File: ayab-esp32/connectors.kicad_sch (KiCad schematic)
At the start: 0 parts

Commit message: first draft schematic
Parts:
- added J602: 900_SOLENOIDS_A, symbol Connector_Generic:Conn_01x10
- added J603: 900_SOLENOIDS_B, symbol Connector_Generic:Conn_01x08
- added J604: USER_I2C, symbol Connector_Generic:Conn_01x04
- added J605: USER_SPI, symbol Connector_Generic:Conn_01x05
- added J606: 910_SOLENOIDS_A, symbol Connector_Generic:Conn_01x10
- added J607: 910_SOLENOIDS_B, symbol Connector_Generic:Conn_01x08
- added J608: 910_ENCODERS_EOL_R, symbol Connector_Generic:Conn_01x10
- added J609: USER_UART, symbol Connector_Generic:Conn_01x04
- added J610: 930_SOLENOIDS_A, symbol Connector_Generic:Conn_01x10
- added J611: 930_SOLENOIDS_B, symbol Connector_Generic:Conn_01x08
- added J612: 930_910_EOL_L, symbol Connector_Generic:Conn_01x03
- added J613: 930_EOL_R, symbol Connector_Generic:Conn_01x03
- added J614: 930_ENCODERS, symbol Connector_Generic:Conn_01x05
- added J615: 965_EOL_L, symbol Connector_Generic:Conn_01x03
- added J616: 965_EOL_R, symbol Connector_Generic:Conn_01x03
- added J617: 965_ENCODERS, symbol Connector_Generic:Conn_01x05
- added R602, R603: 5.1k, symbol Device:R_Small_US
- added R604, R605: 10k, symbol Device:R_Small_US
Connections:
- net ENC_BELTPHASE: now also J608.6 (Pin_6), J614.5 (Pin_5), J617.5 (Pin_5)
- net ENC_V1: now also J608.4 (Pin_4), J614.4 (Pin_4), J617.4 (Pin_4)
- net ENC_V2: now also J608.5 (Pin_5), J614.3 (Pin_3), J617.3 (Pin_3)
- net EOL_L: now also J612.3 (Pin_3), J615.3 (Pin_3)
- net EOL_R: now also J608.8 (Pin_8), J613.3 (Pin_3), J616.3 (Pin_3)
- net I2C_SCL: now also J604.4 (Pin_4), R602.2
- net I2C_SDA: now also J604.2 (Pin_2), R603.2
- new net +12V: J602.10 (Pin_10), J602.9 (Pin_9), J606.10 (Pin_10), J606.9 (Pin_9), J610.10 (Pin_10), J610.9 (Pin_9)
- new net +5V: J604.1 (Pin_1), J605.1 (Pin_1), J608.1 (Pin_1), J609.1 (Pin_1), J612.1 (Pin_1), J613.1 (Pin_1), J614.1 (Pin_1), J615.1 (Pin_1), J616.1 (Pin_1), J617.1 (Pin_1), R602.1, R603.1, R604.1, R605.1
- new net EOL_R_LC: J608.7 (Pin_7), R605.2
- new net GND: J604.3 (Pin_3), J605.5 (Pin_5), J608.10 (Pin_10), J608.2 (Pin_2), J608.9 (Pin_9), J609.4 (Pin_4), J612.2 (Pin_2), J613.2 (Pin_2), J614.2 (Pin_2), J615.2 (Pin_2), J616.2 (Pin_2), J617.2 (Pin_2)
- new net SOL_0: J602.8 (Pin_8), J606.8 (Pin_8), J610.8 (Pin_8)
- new net SOL_1: J602.7 (Pin_7), J606.7 (Pin_7), J610.7 (Pin_7)
- new net SOL_2: J602.6 (Pin_6), J606.6 (Pin_6), J610.6 (Pin_6)
- new net SOL_3: J602.5 (Pin_5), J606.5 (Pin_5), J610.5 (Pin_5)
- new net SOL_4: J602.4 (Pin_4), J606.4 (Pin_4), J610.4 (Pin_4)
- new net SOL_5: J602.3 (Pin_3), J606.3 (Pin_3), J610.3 (Pin_3)
- new net SOL_6: J602.2 (Pin_2), J606.2 (Pin_2), J610.2 (Pin_2)
- new net SOL_7: J602.1 (Pin_1), J606.1 (Pin_1), J610.1 (Pin_1)
- new net SOL_8: J603.8 (Pin_8), J607.8 (Pin_8), J611.8 (Pin_8)
- new net SOL_9: J603.7 (Pin_7), J607.7 (Pin_7), J611.7 (Pin_7)
- new net SOL_A: J603.6 (Pin_6), J607.6 (Pin_6), J611.6 (Pin_6)
- new net SOL_B: J603.5 (Pin_5), J607.5 (Pin_5), J611.5 (Pin_5)
- new net SOL_C: J603.4 (Pin_4), J607.4 (Pin_4), J611.4 (Pin_4)
- new net SOL_D: J603.3 (Pin_3), J607.3 (Pin_3), J611.3 (Pin_3)
- new net SOL_E: J603.2 (Pin_2), J607.2 (Pin_2), J611.2 (Pin_2)
- new net SOL_F: J603.1 (Pin_1), J607.1 (Pin_1), J611.1 (Pin_1)
- new net SPI_CIPO: J605.4 (Pin_4)
- new net SPI_COPI: J605.3 (Pin_3)
- new net SPI_CS: J605.2 (Pin_2), R604.2
- new net UART_RX: J609.3 (Pin_3)
- new net UART_TX: J609.2 (Pin_2)
- no-connect marks 0 -> 1
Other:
- note added: "KH-900"
- note added: "KH-910"
- note added: "KH-930"
- note added: "KH-965"
- note added: "USER EXPANSION"
- note added: "pin 7: see github ayab-hardware #19"
- note added: "shared with which machine?"
- note added: "should reverse engineer pins 9,10"
- note added: "should we use qwiic connector?"
- company: (none) -> matei
- title: (none) -> CONNECTORS

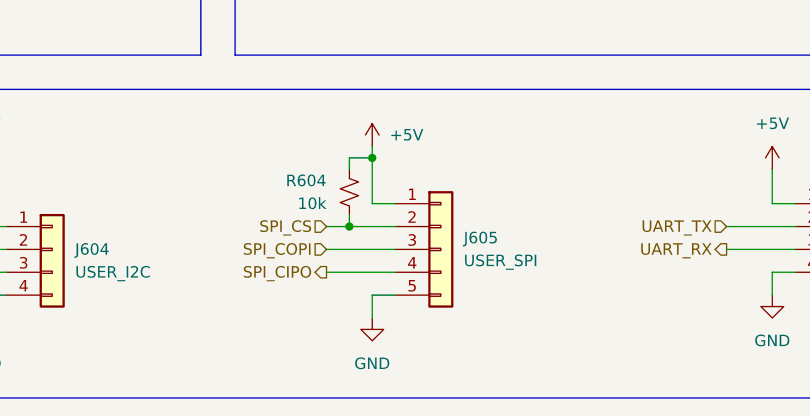
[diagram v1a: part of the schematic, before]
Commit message: add spi_sck line
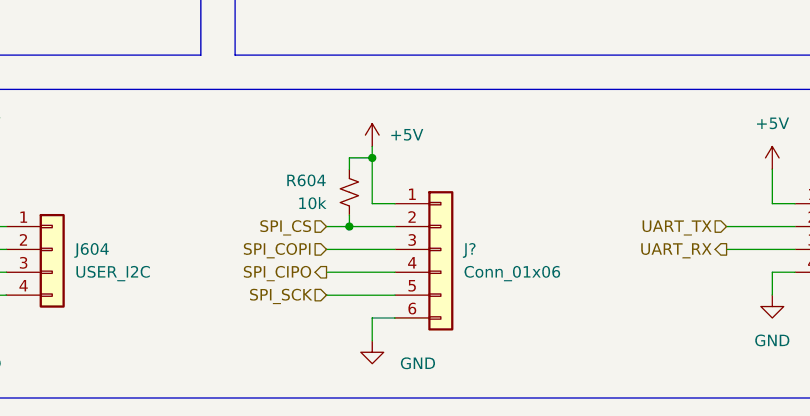
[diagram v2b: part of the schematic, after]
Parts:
- removed J605: USER_SPI, symbol Connector_Generic:Conn_01x05
- added J?: Conn_01x06, symbol Connector_Generic:Conn_01x06
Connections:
- net +5V: now also J?.1 (Pin_1)
- net GND: now also J?.6 (Pin_6)
- net SPI_CIPO: now also J?.4 (Pin_4)
- net SPI_COPI: now also J?.3 (Pin_3)
- net SPI_CS: now also J?.2 (Pin_2)
- new net SPI_SCK: J?.5 (Pin_5)
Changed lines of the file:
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@@
     (stroke (width 0) (type default))
   )
-  (wire (pts (xy 100.33 182.88) (xy 97.79 182.88))
+  (wire (pts (xy 100.33 185.42) (xy 97.79 185.42))
     (stroke (width 0) (type default))
   )
@@
     (stroke (width 0) (type default))
   )
-  (wire (pts (xy 97.79 182.88) (xy 97.79 185.42))
+  (wire (pts (xy 97.79 185.42) (xy 97.79 187.96))
     (stroke (width 0) (type default))
   )
@@
     (stroke (width 0) (type default))
   )
+  (wire (pts (xy 92.71 182.88) (xy 100.33 182.88))
+    (stroke (width 0) (type default))
+  )
   (wire (pts (xy 171.45 68.58) (xy 187.96 68.58))
     (stroke (width 0) (type default))
@@
   )
   (hierarchical_label "ENC_BELTPHASE" (shape output) (at 173.99 129.54 180) (fields_autoplaced)
+    (effects (font (size 1.27 1.27)) (justify right))
+  )
+  (hierarchical_label "SPI_SCK" (shape input) (at 92.71 182.88 180) (fields_autoplaced)
     (effects (font (size 1.27 1.27)) (justify right))
   )
@@
         (path "/ad16b75f-afc8-4717-a7c6-8dd7b69a18e2/7cdcbcc1-4c9b-4f2f-a9ba-c3dab0b4149d"
           (reference "J615") (unit 1)
-        )
-      )
-    )
-  )
-  (symbol (lib_id "Connector_Generic:Conn_01x05") (at 105.41 177.8 0) (unit 1)
-    (in_bom yes) (on_board yes) (dnp no) (fields_autoplaced)
-    (property "Reference" "J605" (at 107.95 176.53 0)
-      (effects (font (size 1.27 1.27)) (justify left))
-    )
-    (property "Value" "USER_SPI" (at 107.95 179.07 0)
-      (effects (font (size 1.27 1.27)) (justify left))
-    )
-    (property "Footprint" "" (at 105.41 177.8 0)
-      (effects (font (size 1.27 1.27)) hide)
-    )
-    (property "Datasheet" "~" (at 105.41 177.8 0)
-      (effects (font (size 1.27 1.27)) hide)
-    )
-    (pin "1")
-    (pin "2")
-    (pin "3")
-    (pin "4")
-    (pin "5")
-    (instances
-      (project "ayab-esp32"
-        (path "/ad16b75f-afc8-4717-a7c6-8dd7b69a18e2/7cdcbcc1-4c9b-4f2f-a9ba-c3dab0b4149d"
-          (reference "J605") (unit 1)
         )
       )
@@
     )
   )
-  (symbol (lib_id "power:GND") (at 97.79 185.42 0) (unit 1)
-    (in_bom yes) (on_board yes) (dnp no) (fields_autoplaced)
-    (property "Reference" "#PWR036" (at 97.79 191.77 0)
-      (effects (font (size 1.27 1.27)) hide)
-    )
-    (property "Value" "GND" (at 97.79 190.5 0)
-      (effects (font (size 1.27 1.27)))
-    )
-    (property "Footprint" "" (at 97.79 185.42 0)
-      (effects (font (size 1.27 1.27)) hide)
-    )
-    (property "Datasheet" "" (at 97.79 185.42 0)
+  (symbol (lib_id "power:GND") (at 97.79 187.96 0) (unit 1)
+    (in_bom yes) (on_board yes) (dnp no)
+    (property "Reference" "#PWR036" (at 97.79 194.31 0)
+      (effects (font (size 1.27 1.27)) hide)
+    )
+    (property "Value" "GND" (at 102.87 190.5 0)
+      (effects (font (size 1.27 1.27)))
+    )
+    (property "Footprint" "" (at 97.79 187.96 0)
+      (effects (font (size 1.27 1.27)) hide)
+    )
+    (property "Datasheet" "" (at 97.79 187.96 0)
       (effects (font (size 1.27 1.27)) hide)
     )
@@
         )
       )
+    )
+  )
+  (symbol (lib_id "Connector_Generic:Conn_01x06") (at 105.41 177.8 0) (unit 1)
+    (in_bom yes) (on_board yes) (dnp no) (fields_autoplaced)
+    (property "Reference" "J?" (at 107.95 177.8 0)
+      (effects (font (size 1.27 1.27)) (justify left))
+    )
+    (property "Value" "Conn_01x06" (at 107.95 180.34 0)
+      (effects (font (size 1.27 1.27)) (justify left))
+    )
+    (property "Footprint" "" (at 105.41 177.8 0)
+      (effects (font (size 1.27 1.27)) hide)
+    )
+    (property "Datasheet" "~" (at 105.41 177.8 0)
+      (effects (font (size 1.27 1.27)) hide)
+    )
+    (pin "1")
+    (pin "2")
+    (pin "3")
+    (pin "4")
+    (pin "5")
+    (pin "6")
+    (instances
+      (project "ayab-esp32"
+        (path "/ad16b75f-afc8-4717-a7c6-8dd7b69a18e2/7cdcbcc1-4c9b-4f2f-a9ba-c3dab0b4149d"
+          (reference "J?") (unit 1)
+        )
+      )

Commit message: fix some comments from jpcornil-git
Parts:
- removed R605: 10k, symbol Device:R_Small_US
- added TP?: 10, symbol Connector:TestPoint
- added TP?: 9, symbol Connector:TestPoint
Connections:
- net +5V: no longer J604.1 (Pin_1), J609.1 (Pin_1), J?.1 (Pin_1), R602.1, R603.1, R604.1
- net EOL_R: no longer J608.8 (Pin_8)
- net GND: now also J604.4 (Pin_4); no longer J604.3 (Pin_3), J608.10 (Pin_10), J608.9 (Pin_9)
- net I2C_SCL: now also J604.1 (Pin_1), R603.2; no longer J604.4 (Pin_4), R602.2
- net I2C_SDA: now also R602.2; no longer R603.2
- net UART_RX: now also J609.1 (Pin_1); no longer J609.3 (Pin_3)
- net EOL_R_LC renamed EOL_R_S
- new net: J608.10 (Pin_10), TP?.1
- new net: J608.9 (Pin_9), TP?.1
- new net +3V3: J604.3 (Pin_3), J609.3 (Pin_3), J?.1 (Pin_1), R602.1, R603.1, R604.1
- new net EOL_R_N: J608.8 (Pin_8)
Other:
- moved on the sheet: J604, R602, R603, R604

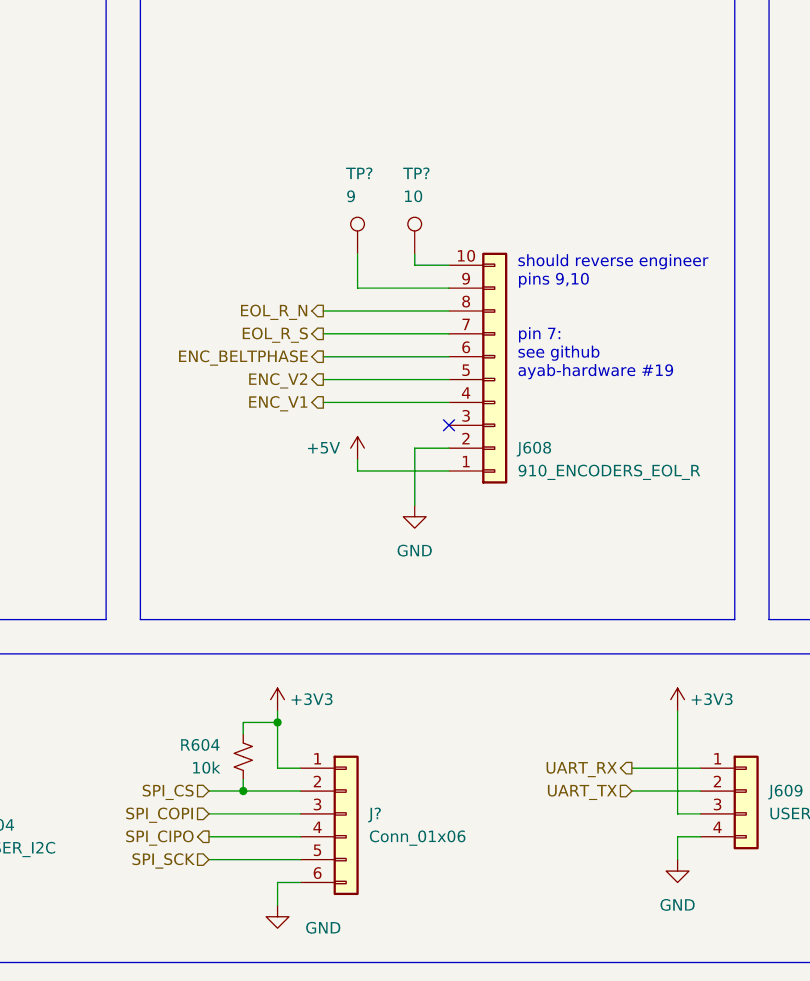
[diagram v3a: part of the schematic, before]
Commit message: add pch MOSFET for polarity protection
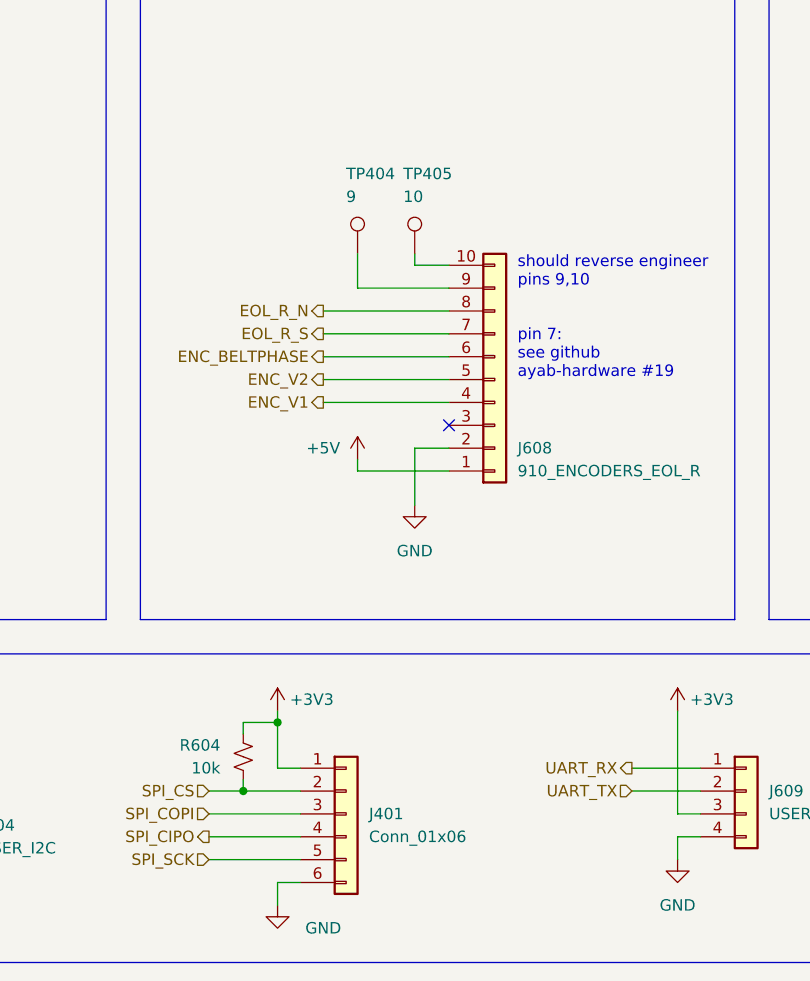
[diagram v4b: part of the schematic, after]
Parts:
- gave numbers to parts that had none: 3
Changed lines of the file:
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@@
   (symbol (lib_id "Connector:TestPoint") (at 113.03 115.57 0) (unit 1)
     (in_bom yes) (on_board yes) (dnp no)
-    (property "Reference" "TP?" (at 111.76 106.68 0)
+    (property "Reference" "TP405" (at 111.76 106.68 0)
       (effects (font (size 1.27 1.27)) (justify left))
     )
@@
       (project "ayab-esp32"
         (path "/ad16b75f-afc8-4717-a7c6-8dd7b69a18e2/7cdcbcc1-4c9b-4f2f-a9ba-c3dab0b4149d"
-          (reference "TP?") (unit 1)
+          (reference "TP405") (unit 1)
         )
       )
@@
   (symbol (lib_id "Connector:TestPoint") (at 106.68 115.57 0) (unit 1)
     (in_bom yes) (on_board yes) (dnp no)
-    (property "Reference" "TP?" (at 105.41 106.68 0)
+    (property "Reference" "TP404" (at 105.41 106.68 0)
       (effects (font (size 1.27 1.27)) (justify left))
     )
@@
       (project "ayab-esp32"
         (path "/ad16b75f-afc8-4717-a7c6-8dd7b69a18e2/7cdcbcc1-4c9b-4f2f-a9ba-c3dab0b4149d"
-          (reference "TP?") (unit 1)
+          (reference "TP404") (unit 1)
         )
       )
@@
   (symbol (lib_id "Connector_Generic:Conn_01x06") (at 105.41 177.8 0) (unit 1)
     (in_bom yes) (on_board yes) (dnp no) (fields_autoplaced)
-    (property "Reference" "J?" (at 107.95 177.8 0)
+    (property "Reference" "J401" (at 107.95 177.8 0)
       (effects (font (size 1.27 1.27)) (justify left))
     )
@@
       (project "ayab-esp32"
         (path "/ad16b75f-afc8-4717-a7c6-8dd7b69a18e2/7cdcbcc1-4c9b-4f2f-a9ba-c3dab0b4149d"
-          (reference "J?") (unit 1)
-        )
-      )
+          (reference "J401") (unit 1)
+        )
+      )

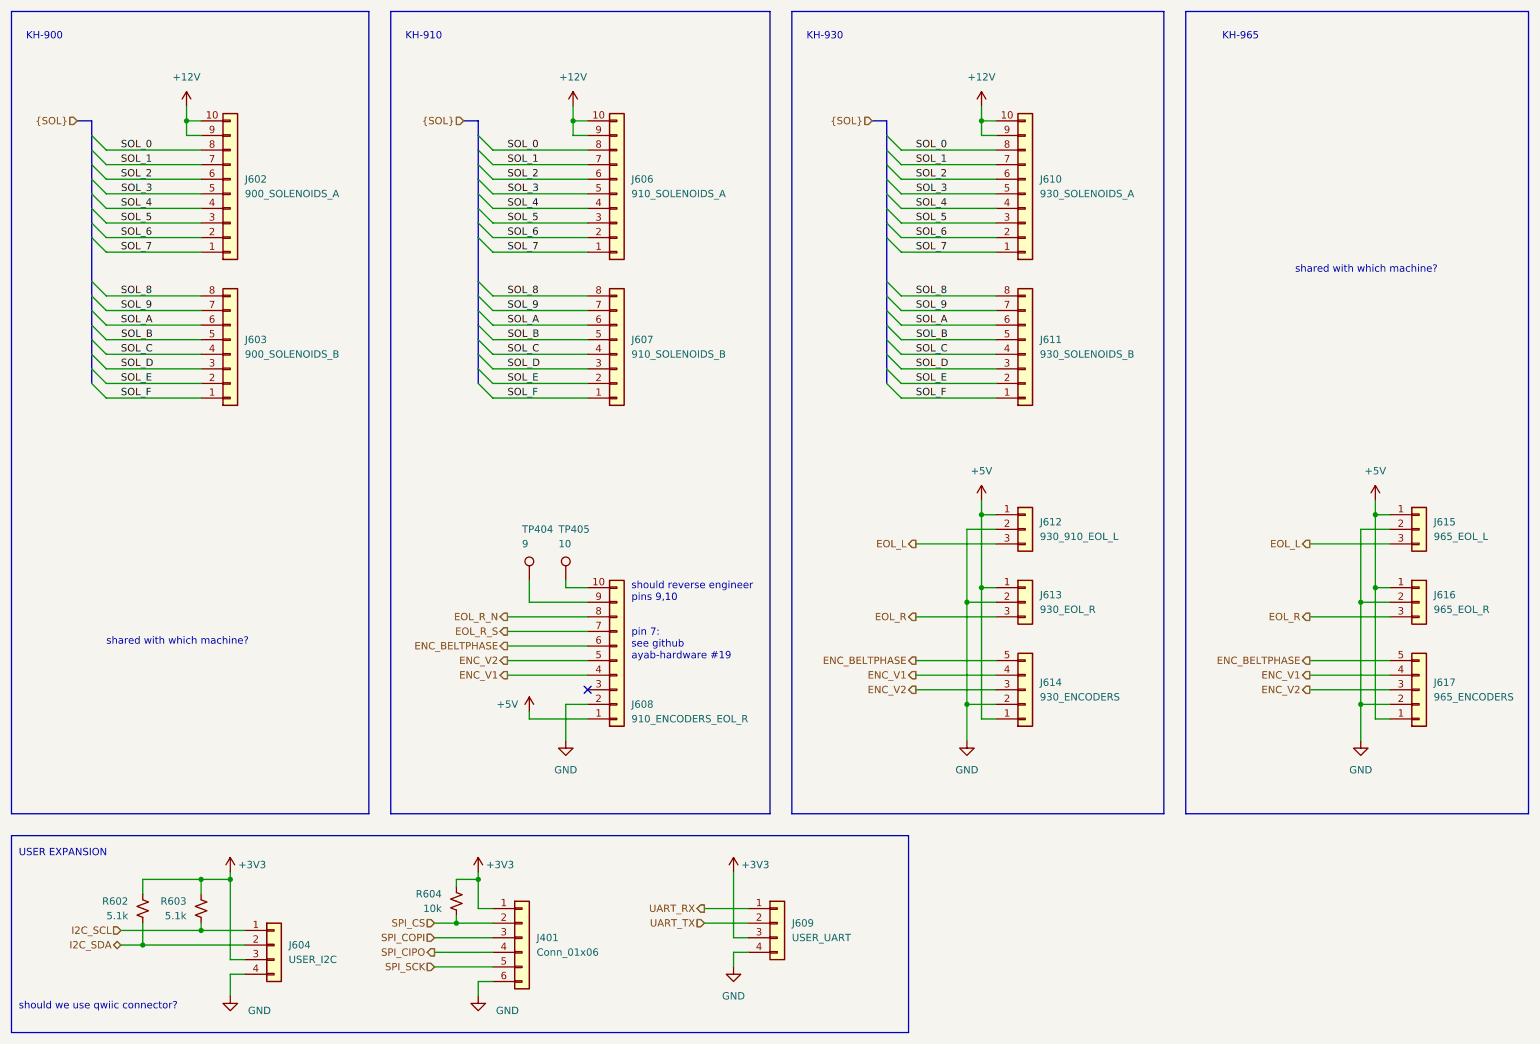
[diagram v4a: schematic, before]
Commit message: add ideal diode, remove extra uln2003a, add comparator for analog EOL sensors
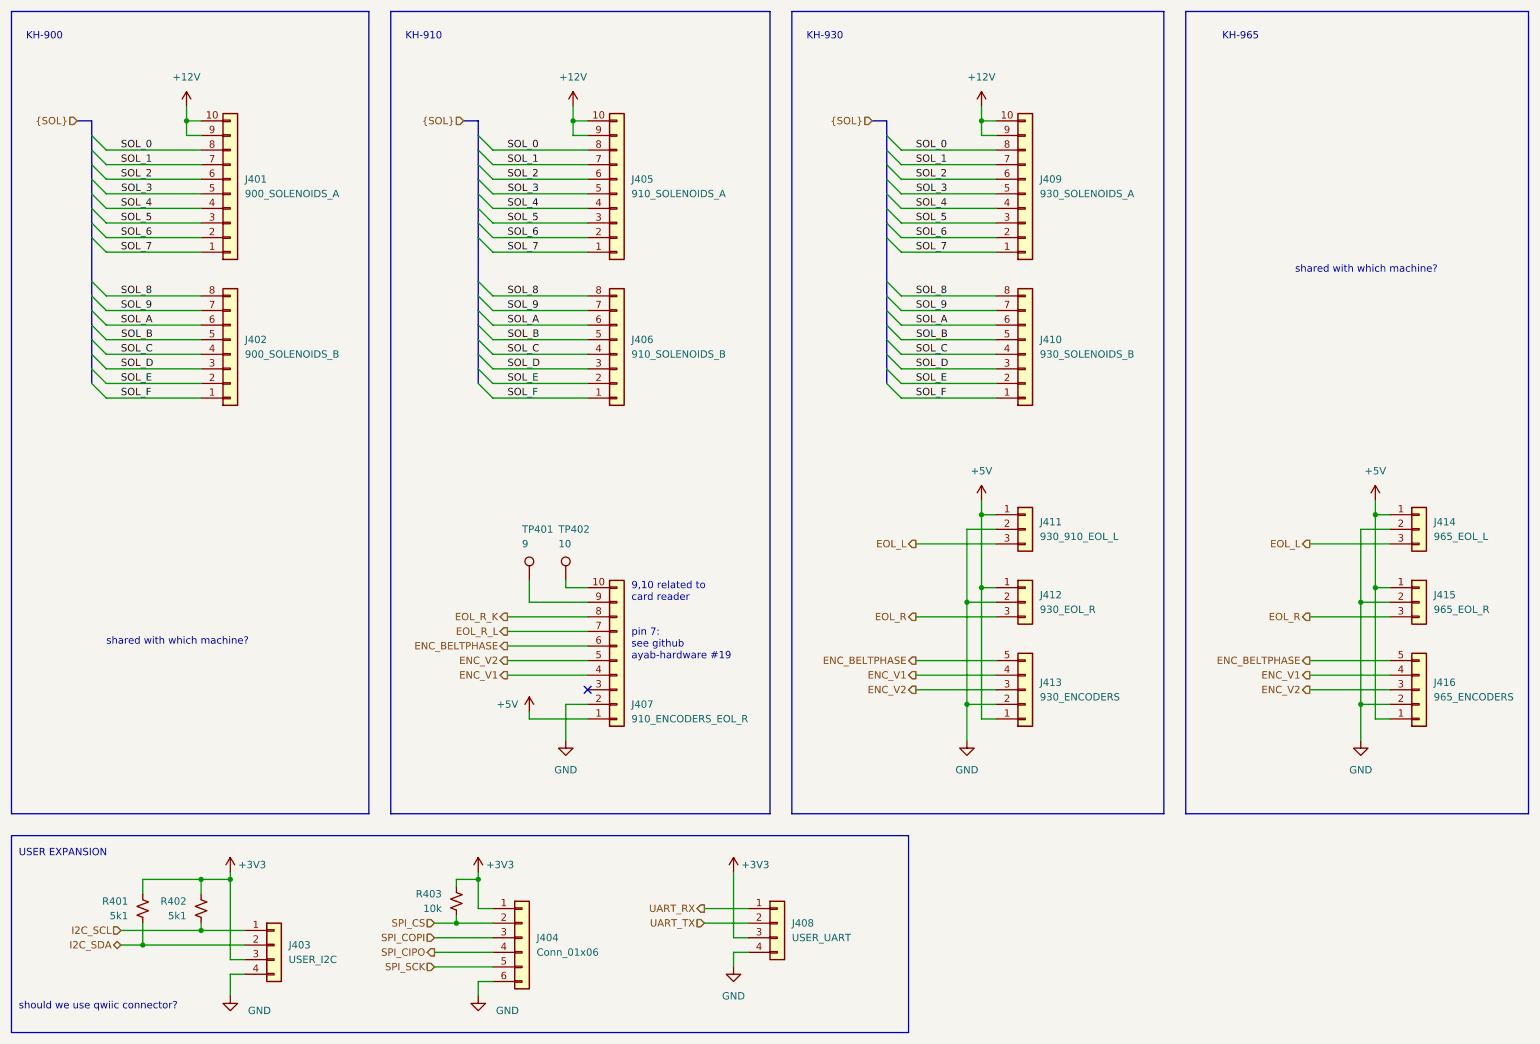
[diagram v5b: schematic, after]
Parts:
- R401: renamed from R602; value 5.1k -> 5k1
- R402: renamed from R603; value 5.1k -> 5k1
- renumbered J602 to J401, J603 to J402, J604 to J403, J401 to J404, J606 to J405, J607 to J406, J608 to J407, J609 to J408, J610 to J409, J611 to J410, J612 to J411, J613 to J412, J614 to J413, J615 to J414, J616 to J415, J617 to J416, R604 to R403, TP404 to TP401, TP405 to TP402
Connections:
- net EOL_R_N renamed EOL_R_K
- net EOL_R_S renamed EOL_R_L
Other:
- note added: "9,10 related to card reader"
- note removed: "should reverse engineer pins 9,10"
